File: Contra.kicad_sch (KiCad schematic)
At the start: 5 parts, among them J1 Conn_01x04, J2 Conn_01x02, SW1 SW_PUSH, SW2 SW_SPDT, U1 ProMicro

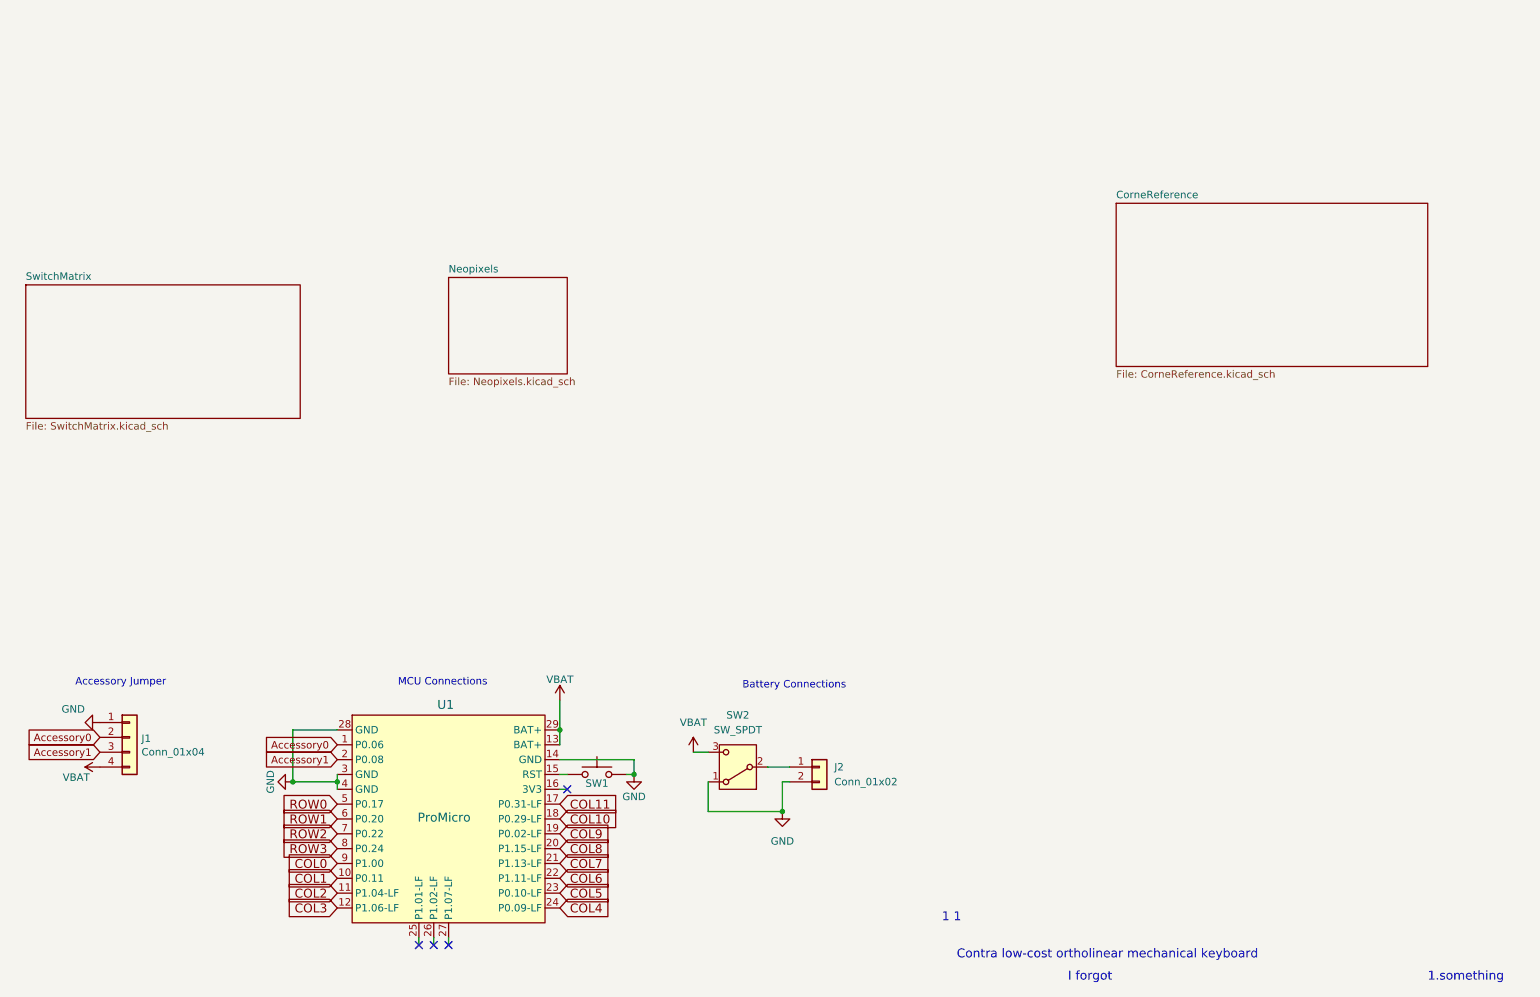
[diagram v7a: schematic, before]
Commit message: Place keyswitches in grid
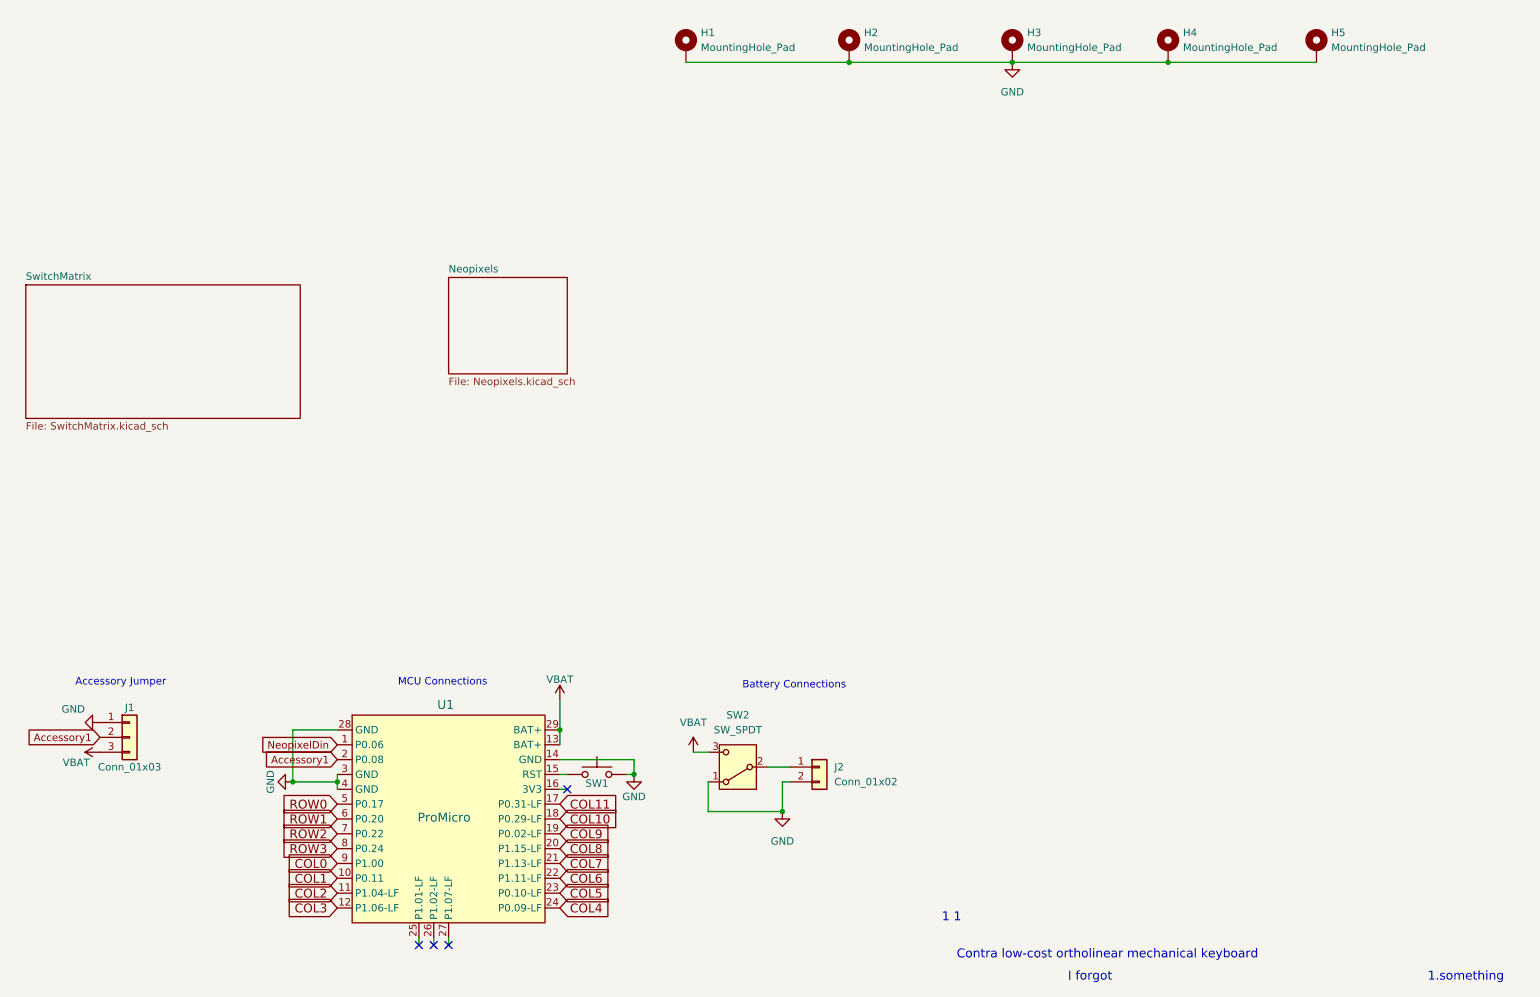
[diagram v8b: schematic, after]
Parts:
- added H1, H2, H3, H4, H5: MountingHole_Pad, MountingHole:MountingHole_2.2mm_M2_Pad, symbol Mechanical:MountingHole_Pad
- J1: value Conn_01x04 -> Conn_01x03; footprint Connector_PinHeader_2.54mm:PinHeader_1x04_P2.54mm_Horizontal -> Connector_PinHeader_2.54mm:PinHeader_1x03_P2.54mm_Horizontal; symbol Connector_Generic:Conn_01x04 -> Connector_Generic:Conn_01x03
- U1: footprint PCM_marbastlib-xp-promicroish:nice_nano_AH_USBup -> Reilly_Components:SuperMini NRF52840
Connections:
- net Accessory1: now also J1.2 (Pin_2); no longer J1.3 (Pin_3)
- net GND: now also H1.1, H2.1, H3.1, H4.1, H5.1
- net VBAT: now also J1.3 (Pin_3); no longer J1.4 (Pin_4)
- net Accessory0 renamed NeopixelDin
- net NeopixelDin: no longer J1.2 (Pin_2)
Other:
- removed sheet CorneReference
